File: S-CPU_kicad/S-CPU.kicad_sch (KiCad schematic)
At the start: 374 parts, among them U6 IAOO1, U8 IAOO0

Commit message: Progress in DMA section. Fixed some DFF output issues.
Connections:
- net wOCLX is gone; now on net ~{DMA_BUS_ON}: KBWU.1 (IN), KBWU.3 (IN)
- net ~{DMA_BUS_ON}: now reaches BCDB.3, CBIS.1, KBTI.1, OCLX.6 (Q)
- net 21XX_DMA_RD renamed DMA_WR
- net DMA_CLK? renamed DMA_CLK
- net DMA_ON? renamed DMA_ON
- net DMA_RW renamed DMA_B->A
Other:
- sheet DMA ports: added DMA_OFF, DMA_ON, wCSDS, wCSGZ, wDSKP, wNBEB_wNBEG_XIN/8, wOBXZ_wOCHV_~{XIN/2}, wPOSD, wQKAG5, wSKDK, wUKYL, wVOLG, wWOCA, wWOVT, wWOWE, wXKGP, wXOAO, wXOWO, ~{wZOOJ}; removed wOAFI_wOACU_XIN/4, wOBXZ_wOCHV_XIN/2
- moved on the sheet: OCLC, OCLX, OMRS

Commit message: Update in DMA sections - most debug signals identified. Error found in SYS clk generation. Simulation show correct 6, 8 and 12 cycle SYSCLK modes.
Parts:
- removed JAKD: NOR_3, symbol Ricoh_Cells:NOR_3
- removed PAWH: AND_2, symbol Ricoh_Cells:AND_2
- added JAKD: OAI_21, symbol Ricoh_Cells:OAI_21
- added PAWH, ROMA: NAND_2, symbol Ricoh_Cells:NAND_2
- added ROLZ: AND_2, symbol Ricoh_Cells:AND_2
- added ZOZP: INVERTER_A, symbol Ricoh_Cells:INVERTER_A
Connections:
- net 6_CYCLES: now also JAHF.2, JAQD.6 (Q), JAKD.1; no longer CABL.5, HAUU0.2
- net MODE4_OR_MODE5: now also ROMA.2
- net wDBJW_wHASI_RST: now also PAWH.1
- net ~{MODE0_OR_MODE6}: now also ROLZ.2
- net ~{wRDY}: now also ZOZP.1
- net at PBAD.6 (Q): now also PAWH.2
- net at MAJY.3: now also MAOG.2 (D); no longer KAEZ.2 (D)
- net at PAWC.4 (RESET): now also PAWH.3
- net at JAGY.2, JAHF.1: now also JAKD.3
- net at MAHR.3: now also KAEZ.2 (D); no longer MAOG.2 (D)
- net at KAHG.1: now also JAKD.4
- net CONTROLLER renamed 12_CYCLES
- net 12_CYCLES: now also JAKD.2
- net FALLING_VBLANK renamed LONG_FALLING_VBLANK
- net wJAXO renamed SYNCED_REFRESH_EN
- new net: CABL.5, HAUU0.2
- new net: ROMA.1, ZOZP.2
- new net: ROLZ.1, ROMA.3
- no-connect marks 22 -> 23
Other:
- sheet DMA ports: added GDMA_TRANSFER; removed wPOSD
- sheet OTHER_42XX_REGISTERS ports: added LONG_FALLING_VBLANK; removed RISING_VBLANK
- note added: "420D WRITE FAST ROM ENABLE"
- note added: "Address decoding"
- note added: "Cells in DMA section but not connected. Change of design or test in early prototypes?"
- note added: "DRAM Refresh"
- note added: "Inverted SYSCLK with 1 cycle delay"
- note added: "Latches 65816 Addresses on 2nd cycle of SYSCLK. Disabled during DMA and permanently latched in MODE7"
- note added: "OAGE is MUL DIV SYSCLK"
- note added: "RAM and RAM Selection"
- note added: "SYSCLK Generation"
- note removed: "420D WRITE"
- note removed: "CPU clock (1 -> 0)"
- note removed: "Checked items"
- note removed: "Goes to DMA too"
- note removed: "Latches 65816 Addresses on first half of CPU clock period, normally off during DMA and permanently latched in MODE7"
- note removed: "OAGE is MUL DIV CLK"
- note removed: "To bottom section"
- note removed: "When wJBDJ is set to 0 it might force 6502 emulation mode since wJBDJ can only be low in MODE 2 or 3"
- moved on the sheet: AABC, AAFD, AAVE, AAXD, ABORT, ACKS, BAAG, BABW, BAEH, BAGU, BAIS, BALC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

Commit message: Schematics update.
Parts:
- removed AABC, AABZ, BAAG, BAAO, BABK, BABL, CACL, CAFH, DBIS, DBJW, DBPI, DBPP, DBVA, FBTA, GAJP, HAKW, HASI, HAXK, HBPL, IBEP, IBUD, JBDJ, JBIL, JBQK, LCIH, MAGR, MAGV, MASS, MAWK, MBCD, MBSK, NAGK, NAJD, NAQE, NBBM, NBEB, NBEG, NBHJ, NBHM, NBKW, NBPG, NBQA, NBRL, OACU, OAFI, OAFM, OAGC, OAGE, OANZ, OATI, OBXZ, OCHV, OCOG, OCRQ, OCRS, ODIB, ODQC, ODSN, OEAE: BUF, symbol Ricoh_Cells:BUF
- removed AAFD, BALC, BANP, FBFE, GBEI, HALC, HBCT, HBGA, IANF, IAQU, IBGG, IBKU, IBUA, JBCR, KBVA, KBWT, LBOQ, LBQM, MAHR, MAJY, MAWW, MBDX, MBZG, NBJW, NBUB, NBZA, NCAN, OAHW: OR_2, symbol Ricoh_Cells:OR_2
- removed AAHT, AAKO, BAGU, BBAR, EBQY, IAQD, IAQV, JAHF, JAXC, KAHG, LCSG, MAAG, MABB, MAVB, NAPZ, NBCF, NBEP, NBIE, OALA, OBEQ, OCEG, OCQI, OCVK, PASU, QBOC, ROLZ: AND_2, symbol Ricoh_Cells:AND_2
- removed AAJX, AALV, BAOZ, BBUI, CAEO, DADO, KBPI: NAND_4, symbol Ricoh_Cells:NAND_4
- removed AAMX, BABW, BANW, BAUV, BAYS, BBQF, BBXY, BBYP, CADW, CAEI, CAWE, CAZC, CBIS, DCDY, DCIN, EAHW, EARJ, EASO, EBBE, EBMJ, EBMQ, EBOS, EFED, FBBC, FBPE, HANA, HAZL, HBQJ, IAQS, IAUB, IBNJ, JAGY, JAWP, JAXB, JBDE, JBRX, KAAQ, KBSI, KBTI, LBWH, LBYR, LCLR, LDAD, MAGI, MAMK, MBBX, MBNS, MBUB, NAPN, OAAF, OBBW, OBEA, OBRC, OBXF, OBXV, OCFG, ODYH, OMRS, ZOZP: INVERTER_A, symbol Ricoh_Cells:INVERTER_A
- removed AAVE, BBFY, BBHQ, CAWC, CAXW: XNOR, symbol Ricoh_Cells:XNOR
- removed AAXD, BAEH, BAEW, BAFF, BBKM, EACZ, EFEL, IARQ, IBPY, JBSU, LCQZ: NOR_2, symbol Ricoh_Cells:NOR_2
- removed ABORT, HALT, HVCM, RDY, RES, TCKSEL0, TCKSEL1, TM, UNCONNECTEDPIN, XIN, ~{DRAMMODE}: IBUF, symbol Ricoh_Cells:IBUF
- removed ACKS, GBEG, IARF, LCSU, MBPY, MCCZ: OR_3, symbol Ricoh_Cells:OR_3
- removed ACLK, CPUCK, MF, REFRESH, VP, XF, ~{CPU_RD}, ~{CPU_WR}, ~{DMA}, ~{ML}, ~{PARD}, ~{PAWR}, ~{RAM_SEL}, ~{ROM_SEL}: OBUF_A, symbol Ricoh_Cells:OBUF_A
- removed ACPQ, DCQF, DFAA, DFAF, EBRW, GBGK, GFAY, GFCD, IAAG: DELAY_BUF, symbol Ricoh_Cells:DELAY_BUF
- removed BAIS: OR_4, symbol Ricoh_Cells:OR_4
- removed BANX, BBWK, FFCV, FFGS, HAAI, JBND, JBPY, KBUP, LCLC, MBRP, MBXS, NBZE, OATK, OBNR, OCSD, PAWH, ROMA: NAND_2, symbol Ricoh_Cells:NAND_2
- removed BAPI, BASL, BATZ, EBCS, GBEV, KBOI, LCNI, LCPE, LCQL, LCQV, MCBW: NAND_3, symbol Ricoh_Cells:NAND_3
- removed BBER, CACT, CACW, CAHN: AND_3, symbol Ricoh_Cells:AND_3
- removed BBKY, CAJX: NOR_3, symbol Ricoh_Cells:NOR_3
- removed BBNU, EAMV, EANE: NOR_5, symbol Ricoh_Cells:NOR_5
- removed BBNW, EAVX, ESOJ, ESQB, IAUO, IAYI, IBAL, JAFF, JAOO, JAQD, JBHT, KAEZ, KAVS, KAYP, KBGM, KBGO, KBIE, KBIF, KBKC, KBLJ, KBMV, OAOU, OCLC, OCLX, PBAD, PBEG: DFFR_A, symbol Ricoh_Cells:DFFR_A
- removed BBSQ, BBZQ, FBII: NAND_5, symbol Ricoh_Cells:NAND_5
- removed BBZX, FBAC: AOI_14, symbol Ricoh_Cells:AOI_14
- removed BCDB, OCDM: AOI_33, symbol Ricoh_Cells:AOI_33
- removed BCFJ, KARA: AND_4, symbol Ricoh_Cells:AND_4
- removed BCGJ, CBAM: XOR, symbol Ricoh_Cells:XOR
- removed CABL, JBNA: OAI_112, symbol Ricoh_Cells:OAI_112
- removed CAKS, CAKW, CANH, CAQL, CBDC, CBEP, CBFI, CBGC, MAOG, MBFM, MBLO, NBIV, NBIZ, NBSM, NBWF, OBHN, OBIW: DFFR_B, symbol Ricoh_Cells:DFFR_B
- removed CARY, CAZD, EAOI: NOR_6, symbol Ricoh_Cells:NOR_6
- removed CAXV: NOR_4, symbol Ricoh_Cells:NOR_4
- removed DCEG, FBSI, IBTS: TRI_INV_IF2, symbol Ricoh_Cells:TRI_INV_IF2
- removed EAPY: NOR_8, symbol Ricoh_Cells:NOR_8
- removed HAMT, LBXR: D_LATCH_A2, symbol Ricoh_Cells:D_LATCH_A2
- removed HAUU0, HAUU1, JAXO, MAXX, OBWM0, OBWM1: MUX, symbol Ricoh_Cells:MUX
- removed HBCA, HBEP: TRI_INV_IF0, symbol Ricoh_Cells:TRI_INV_IF0
- removed HBFW, HBGC, HBQO, IARB, IOAW, JBSB, KBWU, LCWR, NBXE, OAUS, OCBU, OCIS, ODNR: TRI_BUF_IF0, symbol Ricoh_Cells:TRI_BUF_IF0
- removed IBNQ: DEMUX_2-3, symbol Ricoh_Cells:DEMUX_2-3
- removed JAKD: OAI_21, symbol Ricoh_Cells:OAI_21
- removed KAQE: OAI_13, symbol Ricoh_Cells:OAI_13
- removed KBNZ, NBWJ: BUF_INV, symbol Ricoh_Cells:BUF_INV
- removed MBUP: AOI_22, symbol Ricoh_Cells:AOI_22
- removed OBNU: OAI_2222, symbol Ricoh_Cells:OAI_2222
- removed OCTG: DEMUX_3-8, symbol Ricoh_Cells:DEMUX_3-8
- removed PAWC: NOR_LATCH, symbol Ricoh_Cells:NOR_LATCH
- removed SYSCLK: IOBUF_A, symbol Ricoh_Cells:IOBUF_A
- removed U6: IAOO1, symbol Ricoh_Cells:MUX
- removed U8: IAOO0, symbol Ricoh_Cells:MUX
- removed VDA, VPA: IOBUF_B, symbol Ricoh_Cells:IOBUF_B
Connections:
- no-connect marks 23 -> 0
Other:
- sheet ADDR_AND_DATA_BUSES renamed A-BUS AND B-BUS
- added sheet ADDR BUS CONTROL AND DATA BUS (buscontrol.kicad_sch)
- added sheet CLOCKS AND RESETS (clocks.kicad_sch)
- added sheet RW SIGNALS AND ADDRESS_DECODING (rw_decoding.kicad_sch)
- sheet A-BUS AND B-BUS ports: added DMA_PA[0..7], PA[0..7], ~{DMA_BUS_EN}, ~{MODE5}, ~{MODE6}; removed DATABUS_LATCH, DATAIN_EN, DATAOUT_EN
- sheet DIVISION QUOTIENT REGISTERS ports: added wOAGE_SYSCLK; removed OAGE
- sheet DMA ports: added DMA_A[0..23], DMA_B->A, DMA_PA[0..7], HDMA_EMPTY_SCANLINE_COUNTER, HDMA_RELOAD_FLAG, PATTERN_END, wOCRQ_wOCRS_~{XIN/8}, ~{DMA_BUS_ON}, ~{GDMA_LENGTH_IS_ZERO}; removed A[0..23], DMA_ON, PA[0..7], wDSKP, wUKYL, wWOCA, wXKGP, wXOAO, wXOWO, ~{wZOOJ}
- sheet JOYPADS REGISTERS ports: added wMASS_~{JP_RST}, wNBRL_wNBQA_~{XIN/4}; removed wMASS_RST, wNBRL_wNBQA_XIN/4
- sheet OTHER_42XX_REGISTERS ports: added wNBRL_wNBQA_~{XIN/4}; removed wNBRL_wNBQA_XIN/4
- note removed: "1 x XIN/8"
- note removed: "1 x ~{XIN/256}"
- note removed: "1 x ~{XIN/2}"
- note removed: "1 x ~{XIN/8}"
- note removed: "12 cycle flag?"
- note removed: "2 x XIN/2"
- note removed: "2 x XIN/4"
- note removed: "2 x ~{XIN/4}"
- note removed: "420D WRITE FAST ROM ENABLE"
- note removed: "8 cycle flag?"
- note removed: "Address decoding"
- note removed: "B-BUS select (21XX) when not in MODE2 or 3"
- note removed: "Cells in DMA section but not connected. Change of design or test in early prototypes?"
- note removed: "Connected to Data OUT Bus enable pins ODIB = '0' to present data to external bus"
- note removed: "Connected to Data OUT Bus enable pins ODQC = '0' to read external data bus"
- note removed: "DMA OFF CPU CLK"
- note removed: "DMA registers 4300-437F active low select"
- note removed: "DRAM Refresh"
- note removed: "Disconnects 65816 in MODE7, in MODE1 when RDY is low and during DMA"
- note removed: "External SYSCLK when 1) RDY = 0 and mode 1-5 or 7 2) mode 2-3 or mode 7"
- note removed: "Goes low during internal CPU cycles VDA and VPA are low and DMA is not running"
- note removed: "IO range: x0xx xxxx 0xxx xxxx xxxx xxxx"
- note removed: "Internal registers only"
- note removed: "Inverted SYSCLK with 1 cycle delay"
- note removed: "JBNA = JBQK set to '1' when in MODE2-3, in MODE7, in MODE1 + RDY = 0 or DMA is OFF"
- note removed: "JP regs reset"
- note removed: "Latches 65816 Addresses on 2nd cycle of SYSCLK. Disabled during DMA and permanently latched in MODE7"
- note removed: "Latches exernal input data and data bus"
- note removed: "Low when RDY = 0 in mode 1 or when DMA is on in mode 4-6"
- note removed: "Modes are active low - inputs seems to be active low MODE7 = Test mode with external CPU connections bypassing 65816 MODE4-6 = DMA test modes MODE0 = SNES mode MODE1 = SNES in halt mode where RDY is used to pause the 65816 MODE2-3 = NES modes where 4200-43FF registers are disabled and CPU connections are external as original idea was probably to include the NES CPU on the board"
- note removed: "OAGE is MUL DIV SYSCLK"
- note removed: "RAM and RAM Selection"
- note removed: "RESET"
- note removed: "SNES regs reset"
- note removed: "SYSCLK Generation"
- note removed: "System clocks"
- note removed: "To DMA section and bottom section"
- note removed: "To_bottom_of_chip_too Reg Read occurs when RW = '1', SYSCLK = '1', NOT an internal cycle"
- note removed: "from DMA"
- note removed: "~{0000-1FFF} is WRAM ~{6000-7FFF} is expansion ~{4000-41FF} is controller 0000-7FFF is IO range BOAZ is low when accessing 2000-3FFF range (PPU, APU) and 4200-5FFF range (CPU + DMA) BANP is low when A23 is high but not in IO range i.e. FAST ROM access Therefore CABL will be high to allow 6 master cycles per cpu cycle when CPU accesses fast rom, some IO registers and during internal cycles (provid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"
- note removed: "~{ROMSEL} = ~{A23}.A22.A21.A20.A19.A18.A17 + ~{A22}.~{A15} Consistent with access to: - 00-3F/80-BF:8000-FFFF or - 40-7D/C0-FF:0000-FFFF ~{RAMSEL} = not (~{/A23}.A22.A21.A20.A19.A18.A17 + ~{A22}.~{A15}.~{A14}.~{A13}) Consistent with access to: - 00-3F/80-BF:0000-1FFF or - 7E-7F:0000-FFFF"
- company: Regis Galland -> Author: Regis Galland
- moved on the sheet: OMNN, OMVB, PKFR

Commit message: Schematics tidying in progress.
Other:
- sheet ADDR BUS CONTROL AND DATA BUS ports: added DMA_ON, MODE1_OR_MODE3, MODE2_OR_MODE3, MODE4-6, MODE4_OR_MODE5, MODE5_OR_MODE7, wACLK, wIAYI, wOCOG_~{MODE7}, ~{MODE0_OR_MODE6}, ~{MODE1}, ~{MODE4_OR_MODE6}, ~{MODE4}, ~{MODE5}, ~{MODE6}, ~{wRDY}; removed wKBNZ
- sheet CLOCKS AND RESETS ports: added DMA_ON, SYNCED_REFRESH_EN, wACLK, wDBJW_wHASI_~{RST}, ~{XIN1}; removed MODE2_OR_MODE3, wDBJW_wHASI_RST, wKBNZ, ~{INTERNAL_CYCLE}
- sheet DIVISION QUOTIENT REGISTERS ports: added wACLK, wDBJW_wHASI_~{RST}; removed wDBJW_wHASI_RST, wKBNZ
- sheet JOYPADS REGISTERS ports: added AUTO_JP_READING, JPO0, JPO1, JPO2; removed none
- sheet OTHER_42XX_REGISTERS ports: added AUTO_JP_READING, wDBJW_wHASI_~{RST}, wOCOG_~{MODE7}; removed wDBJW_wHASI_RST
- moved on the sheet: OMNN, OMVB, PKFR

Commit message: Big update on the hierarchical sheet. DMA section update too.
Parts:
- removed OMNN: INVERTER_A, symbol Ricoh_Cells:INVERTER_A
- removed OMVB, PKFR: OR_2, symbol Ricoh_Cells:OR_2
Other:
- sheet A-BUS AND B-BUS renamed A-BUS
- added sheet B-BUS (bbus.kicad_sch)
- added sheet MODES (modes.kicad_sch)
- sheet A-BUS ports: added none; removed DMA_PA[0..7], PA[0..7], ~{MODE5}, ~{MODE6}
- sheet ADDR BUS CONTROL AND DATA BUS ports: added CPU_RW_EN, SYNCED_REFRESH_EN, wMBLO_~{XIN/256}, wSYSCLK, ~{MODE0_OR_MODE1}, ~{MODE0}; removed DATABUS_LATCH, MODE1_OR_MODE3, MODE5_OR_MODE7, ~{INTERNAL_CYCLE}, ~{MODE4_OR_MODE6}, ~{MODE4}, ~{MODE5}, ~{MODE6}
- sheet CLOCKS AND RESETS ports: added CPU_RW_EN, H[0..8], MODE1_OR_MODE3, wMBLO_~{XIN/256}, ~{H128-135}; removed H128-135, RW_EN
- sheet DMA ports: added 420X, A[0..23], CPU_CLK, DMA_ON, FALLING_VBLANK, INTERNAL_SYSCLK, LONG_FALLING_VBLANK, PA[0..7], wDBJW_wHASI_~{RST}, wHBLANK, wJPOUT[0..2], wMAGR_wMAGV, wNAGK_wNAJD, wNBHJ_wNBHM_XIN/2, wNBKW_wNBPG_~{XIN/4}, wOACU_wOAFI_XIN/4, wVBLANK, ~{CPU_RD}, ~{MAWK_WR}, ~{MODE5}; removed DMA_CHAN[0..2], GDMA_TRANSFER, HDMA_EMPTY_SCANLINE_COUNTER, HDMA_RELOAD_FLAG, PATTERN_END, wCSDS, wCSGZ, wNBKW_wNBPG_XIN/4, wQKAG5, wSKDK, wVOLG, wWOVT, wWOWE, ~{DMA_RD}, ~{DMA_WR}, ~{GDMA_LENGTH_IS_ZERO}
- sheet JOYPADS REGISTERS ports: added MODE5_OR_MODE7, wJPOUT[0..2]; removed JPO0, JPO1, JPO2
- sheet OTHER_42XX_REGISTERS ports: added H[0..8], wHBLANK, ~{H128-135}; removed H128-135
- sheet RW SIGNALS AND ADDRESS_DECODING ports: added CPU_RW_EN, wSYSCLK, ~{MODE4_OR_MODE6}; removed DATABUS_LATCH, RW_EN, wOCOG_~{MODE7}
- note removed: "DMA"

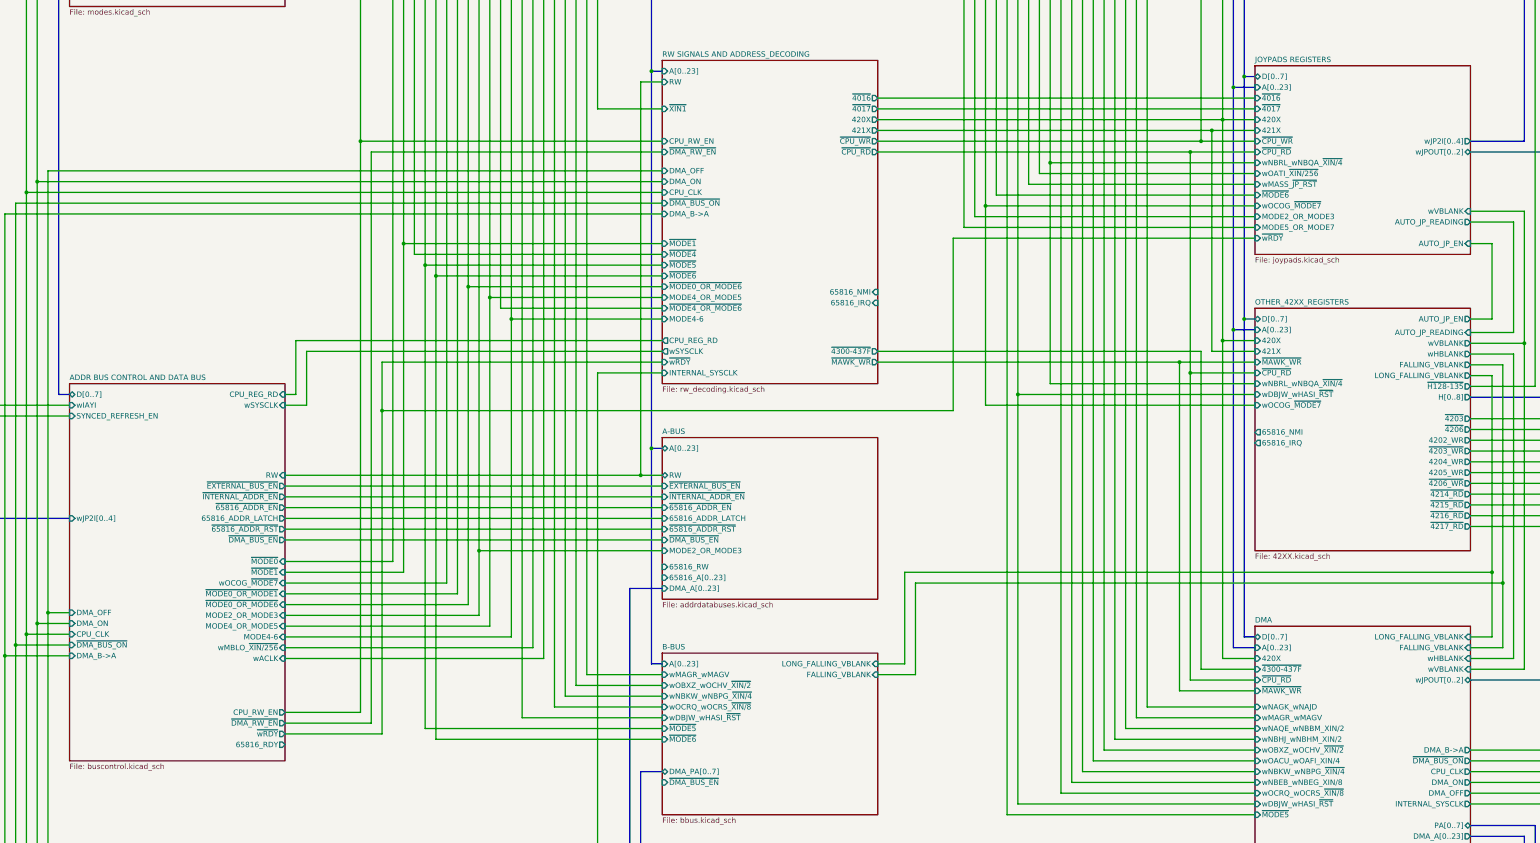
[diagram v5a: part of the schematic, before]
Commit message: DMA section update. Found errors between some MUX and MUXI gates.
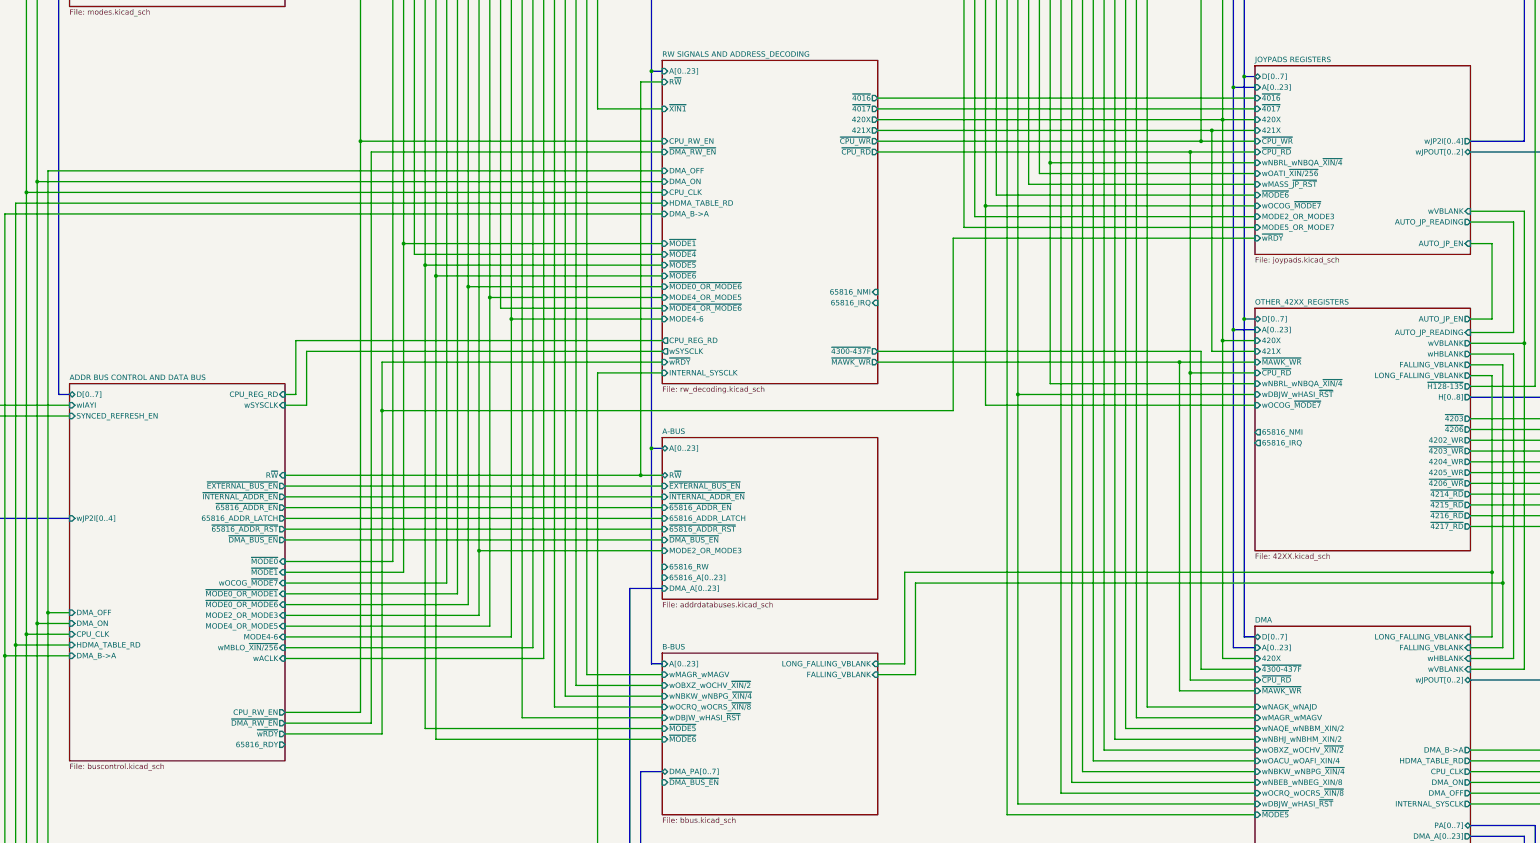
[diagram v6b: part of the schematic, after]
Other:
- sheet A-BUS ports: added R~{W}; removed RW
- sheet ADDR BUS CONTROL AND DATA BUS ports: added HDMA_TABLE_RD, R~{W}; removed RW, ~{DMA_BUS_ON}
- sheet DMA ports: added HDMA_TABLE_RD; removed ~{DMA_BUS_ON}
- sheet RW SIGNALS AND ADDRESS_DECODING ports: added HDMA_TABLE_RD, R~{W}; removed RW, ~{DMA_BUS_ON}
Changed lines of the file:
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@@
       (effects (font (size 1.27 1.27)) (justify left))
     )
-    (pin "~{DMA_BUS_ON}" input (at 76.2 309.245 180)
+    (pin "HDMA_TABLE_RD" input (at 76.2 309.245 180)
       (effects (font (size 1.27 1.27)) (justify left))
     )
@@
       (effects (font (size 1.27 1.27)) (justify left))
     )
-    (pin "RW" input (at 127 269.24 0)
+    (pin "R~{W}" input (at 127 269.24 0)
       (effects (font (size 1.27 1.27)) (justify right))
     )
@@
       (effects (font (size 1.27 1.27)) (justify right))
     )
-    (pin "~{DMA_BUS_ON}" output (at 406.4 336.55 0)
+    (pin "HDMA_TABLE_RD" output (at 406.4 336.55 0)
       (effects (font (size 1.27 1.27)) (justify right))
     )
@@
       (effects (font (size 1.27 1.27)) (justify left top))
     )
-    (pin "RW" input (at 215.9 176.53 180)
+    (pin "R~{W}" input (at 215.9 176.53 180)
       (effects (font (size 1.27 1.27)) (justify left))
     )
@@
       (effects (font (size 1.27 1.27)) (justify left))
     )
-    (pin "~{DMA_BUS_ON}" input (at 215.9 205.105 180)
+    (pin "HDMA_TABLE_RD" input (at 215.9 205.105 180)
       (effects (font (size 1.27 1.27)) (justify left))
     )
@@
       (effects (font (size 1.27 1.27)) (justify left))
     )
-    (pin "RW" tri_state (at 215.9 269.24 180)
-      (effects (font (size 1.27 1.27)) (justify left))
-    )
+    (pin "R~{W}" tri_state (at 215.9 269.24 180)
+      (effects (font (size 1.27 1.27)) (justify left))
+    )

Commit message: Fix ERC errors in schematics.
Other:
- added sheet 65C816 (65c816.kicad_sch)
- sheet ADDR BUS CONTROL AND DATA BUS ports: added 65816_IN[0..1], 65816_PHI2, 65816_VDA, 65816_VPA, 65816_~{RST}, wIAYI_~{RST}, wIBPY, wNBHJ_wNBHM_XIN/2, ~{MODE4}; removed wIAYI
- sheet B-BUS ports: added PA[0..7]; removed none
- sheet CLOCKS AND RESETS ports: added D[0..7], MODE2_OR_MODE3, wIAYI_~{RST}; removed wIAYI
- sheet DIVISION QUOTIENT REGISTERS ports: added MUL_OR_DIV_ON; removed DIV_OR_MUL_ON
- sheet JOYPADS REGISTERS ports: added 65816_BE, 65816_EF, 65816_WAI, wOAXV; removed ~{MODE6}, ~{wRDY}
- sheet OTHER_42XX_REGISTERS ports: added 65816_~{IRQ}, 65816_~{NMI}, wOAXV; removed 65816_IRQ, 65816_NMI
- sheet RW SIGNALS AND ADDRESS_DECODING ports: added 65816_MF, 65816_MLB, 65816_XF, 65816_~{IRQ}, 65816_~{NMI}, MODE2_OR_MODE3, SYNCED_REFRESH_EN, wIBPY, wOATI_~{XIN/256}, wOAXV, ~{DMA_BUS_EN}; removed 65816_IRQ, 65816_NMI
- title: SNES S-CPU Schematics  -> Reverse Engineered SNES S-CPU Schematics 
